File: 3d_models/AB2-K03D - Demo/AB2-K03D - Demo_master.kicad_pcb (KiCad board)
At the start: 2 copper layers, 223 parts

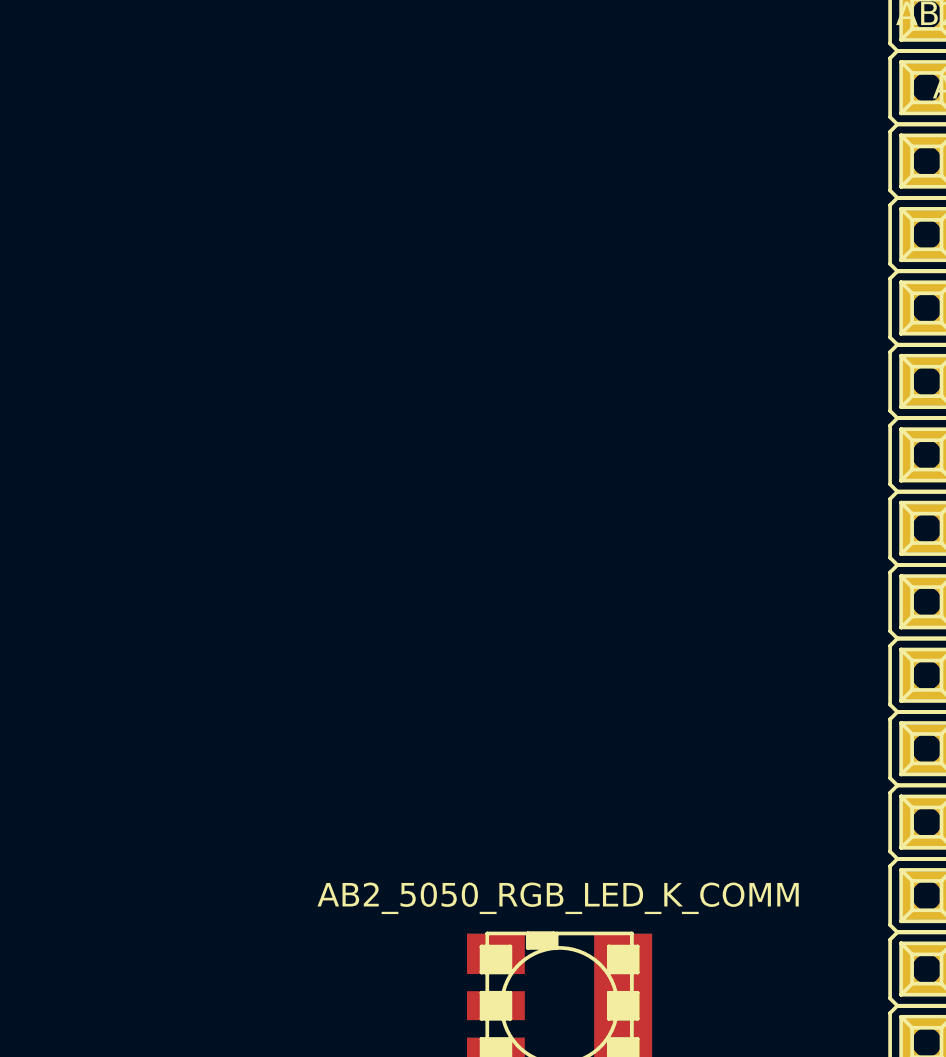
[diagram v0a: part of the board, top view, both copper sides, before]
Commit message: AB2-K03D: add 90' 4mm banana jacks blk/red to master
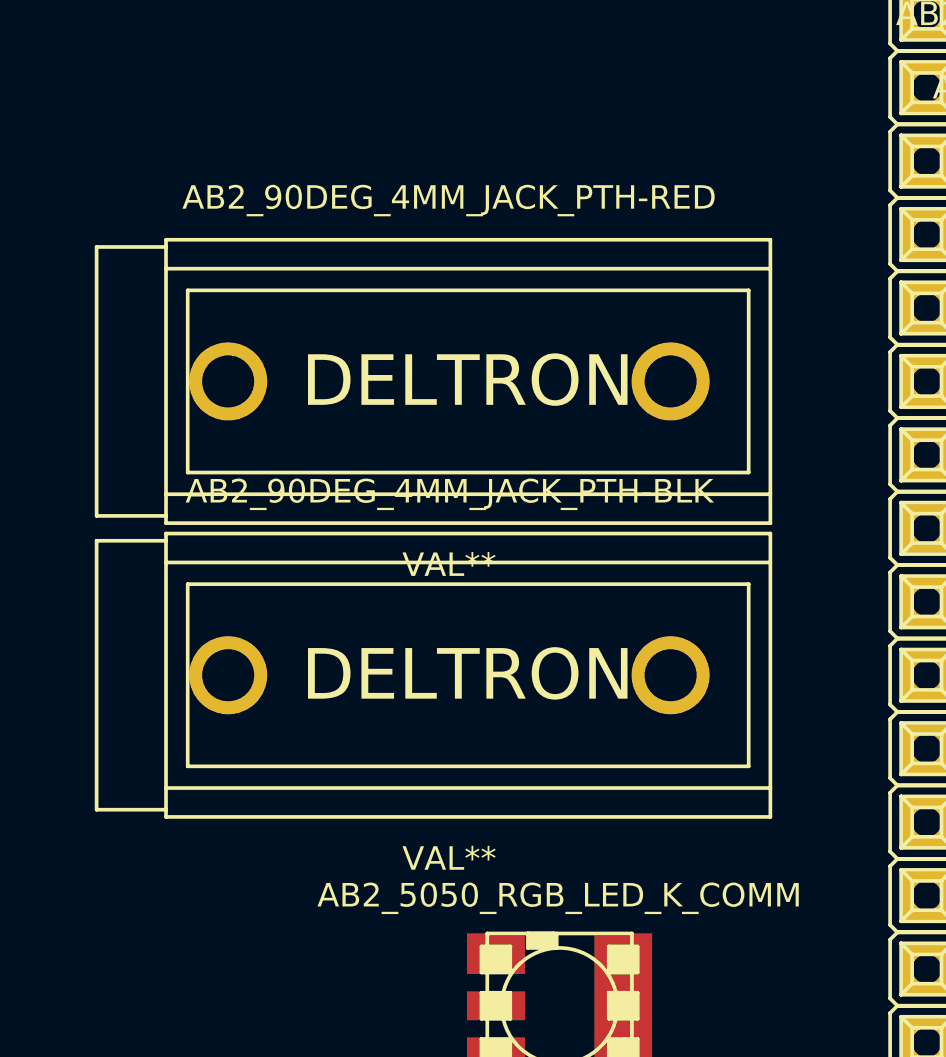
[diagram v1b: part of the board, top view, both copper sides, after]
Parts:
- added AB2_90DEG_4MM_JACK_PTH-BLK: VAL**, AB2_90DEG_4MM_JACK_PTH-BLK, F.Cu at (21.6, 156.2)
- added AB2_90DEG_4MM_JACK_PTH-RED: VAL**, AB2_90DEG_4MM_JACK_PTH-RED, F.Cu at (21.6, 146.1)
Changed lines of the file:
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@@
     (tracks 0)
     (zones 0)
-    (modules 223)
+    (modules 225)
     (nets 1)
   )
@@
     )
   )
+  (module AB2_90DEG_4MM_JACK_PTH-BLK (layer F.Cu)
+    (at 21.59 156.21)
+    (fp_text reference AB2_90DEG_4MM_JACK_PTH-BLK (at 0 -6.35) (layer F.SilkS)
+      (effects (font (size 0.8128 0.8128) (thickness 0.0762)))
+    )
+    (fp_text value VAL** (at 0 6.35) (layer F.SilkS)
+      (effects (font (size 0.8128 0.8128) (thickness 0.0762)))
+    )
+    (fp_line (start -9.05 -3.15) (end 10.35 -3.15) (layer F.SilkS) (width 0.127))
+    (fp_line (start 10.35 -3.15) (end 10.35 3.15) (layer F.SilkS) (width 0.127))
+    (fp_line (start 10.35 3.15) (end -9.05 3.15) (layer F.SilkS) (width 0.127))
+    (fp_line (start -9.05 3.15) (end -9.05 -3.15) (layer F.SilkS) (width 0.127))
+    (fp_line (start -9.8 3.9) (end 11.1 3.9) (layer F.SilkS) (width 0.127))
+    (fp_line (start -9.8 -3.9) (end 11.1 -3.9) (layer F.SilkS) (width 0.127))
+    (fp_text user DELTRON (at 0.635 0) (layer F.SilkS)
+      (effects (font (size 1.75 1.75) (thickness 0.2)))
+    )
+    (fp_line (start -9.8 -4.65) (end -12.2 -4.65) (layer F.SilkS) (width 0.127))
+    (fp_line (start -12.2 -4.65) (end -12.2 4.65) (layer F.SilkS) (width 0.127))
+    (fp_line (start -12.2 4.65) (end -9.8 4.65) (layer F.SilkS) (width 0.127))
+    (fp_line (start -9.8 -4.9) (end -9.8 4.9) (layer F.SilkS) (width 0.127))
+    (fp_line (start -9.8 4.9) (end 11.1 4.9) (layer F.SilkS) (width 0.127))
+    (fp_line (start 11.1 4.9) (end 11.1 -4.9) (layer F.SilkS) (width 0.127))
+    (fp_line (start 11.1 -4.9) (end -9.8 -4.9) (layer F.SilkS) (width 0.127))
+    (pad 1 thru_hole circle (at -7.65 0) (size 2.7 2.7) (drill 1.8)
+      (layers *.Cu *.Mask F.SilkS)
+    )
+    (pad 1 thru_hole circle (at 7.65 0) (size 2.7 2.7) (drill 1.8)
+      (layers *.Cu *.Mask F.SilkS)
+    )
+    (model ../3d_models/ab2_power/AB2_90DEG_4MM_JACK_PTH-BLK.wrl
+      (at (xyz 0 0 0))
+      (scale (xyz 0.3937 0.3937 0.3937))
+      (rotate (xyz 0 0 180))
+    )
+  )
+  (module AB2_90DEG_4MM_JACK_PTH-RED (layer F.Cu)
+    (at 21.59 146.05)
+    (fp_text reference AB2_90DEG_4MM_JACK_PTH-RED (at 0 -6.35) (layer F.SilkS)
+      (effects (font (size 0.8128 0.8128) (thickness 0.0762)))
+    )
+    (fp_text value VAL** (at 0 6.35) (layer F.SilkS)
+      (effects (font (size 0.8128 0.8128) (thickness 0.0762)))
+    )
+    (fp_line (start -9.05 -3.15) (end 10.35 -3.15) (layer F.SilkS) (width 0.127))
+    (fp_line (start 10.35 -3.15) (end 10.35 3.15) (layer F.SilkS) (width 0.127))
+    (fp_line (start 10.35 3.15) (end -9.05 3.15) (layer F.SilkS) (width 0.127))
+    (fp_line (start -9.05 3.15) (end -9.05 -3.15) (layer F.SilkS) (width 0.127))
+    (fp_line (start -9.8 3.9) (end 11.1 3.9) (layer F.SilkS) (width 0.127))
+    (fp_line (start -9.8 -3.9) (end 11.1 -3.9) (layer F.SilkS) (width 0.127))
+    (fp_text user DELTRON (at 0.635 0) (layer F.SilkS)
+      (effects (font (size 1.75 1.75) (thickness 0.2)))
+    )
+    (fp_line (start -9.8 -4.65) (end -12.2 -4.65) (layer F.SilkS) (width 0.127))
+    (fp_line (start -12.2 -4.65) (end -12.2 4.65) (layer F.SilkS) (width 0.127))
+    (fp_line (start -12.2 4.65) (end -9.8 4.65) (layer F.SilkS) (width 0.127))
+    (fp_line (start -9.8 -4.9) (end -9.8 4.9) (layer F.SilkS) (width 0.127))
+    (fp_line (start -9.8 4.9) (end 11.1 4.9) (layer F.SilkS) (width 0.127))
+    (fp_line (start 11.1 4.9) (end 11.1 -4.9) (layer F.SilkS) (width 0.127))
+    (fp_line (start 11.1 -4.9) (end -9.8 -4.9) (layer F.SilkS) (width 0.127))
+    (pad 1 thru_hole circle (at -7.65 0) (size 2.7 2.7) (drill 1.8)
+      (layers *.Cu *.Mask F.SilkS)
+    )
+    (pad 1 thru_hole circle (at 7.65 0) (size 2.7 2.7) (drill 1.8)
+      (layers *.Cu *.Mask F.SilkS)
+    )
+    (model ../3d_models/ab2_power/AB2_90DEG_4MM_JACK_PTH-RED.wrl
+      (at (xyz 0 0 0))
+      (scale (xyz 0.3937 0.3937 0.3937))
+      (rotate (xyz 0 0 180))
+    )
+  )

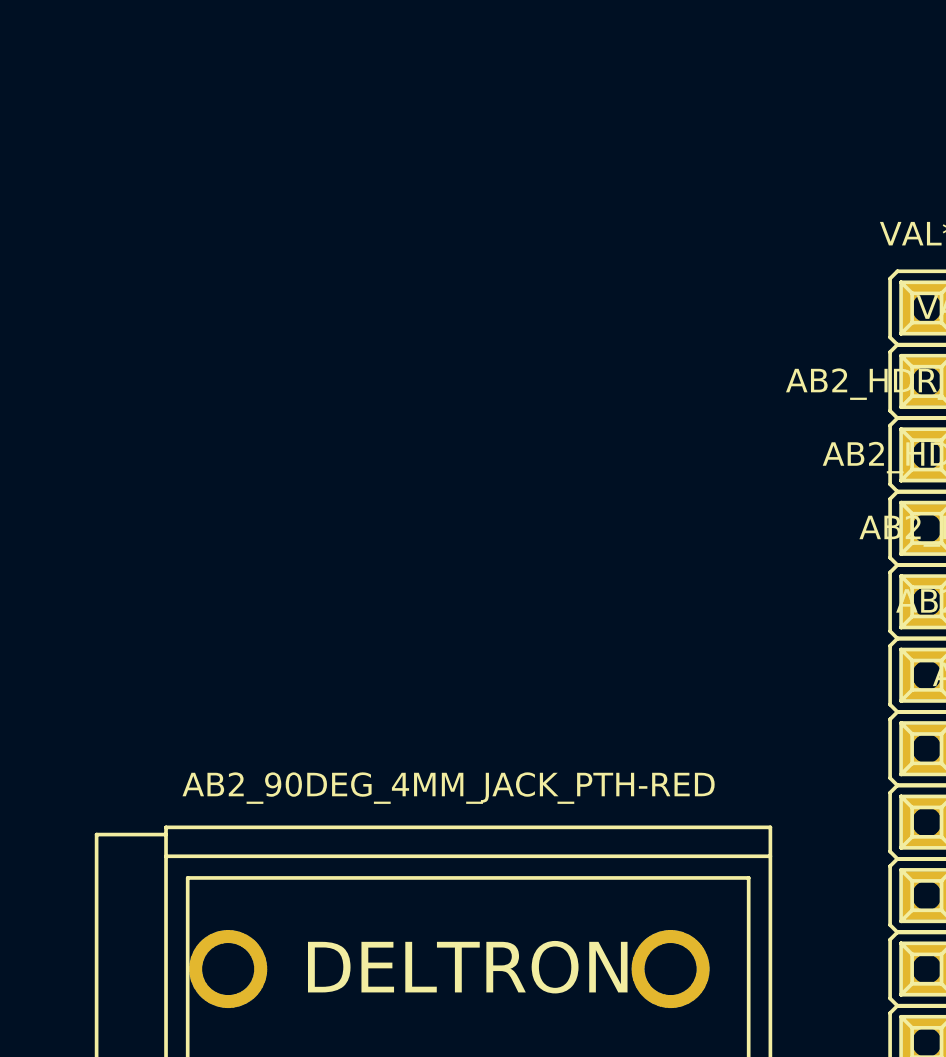
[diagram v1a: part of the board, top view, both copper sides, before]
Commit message: 3d_models: AB2-K03D: add 90' 4mm banana jacks
colors: blk/blu/red/yel
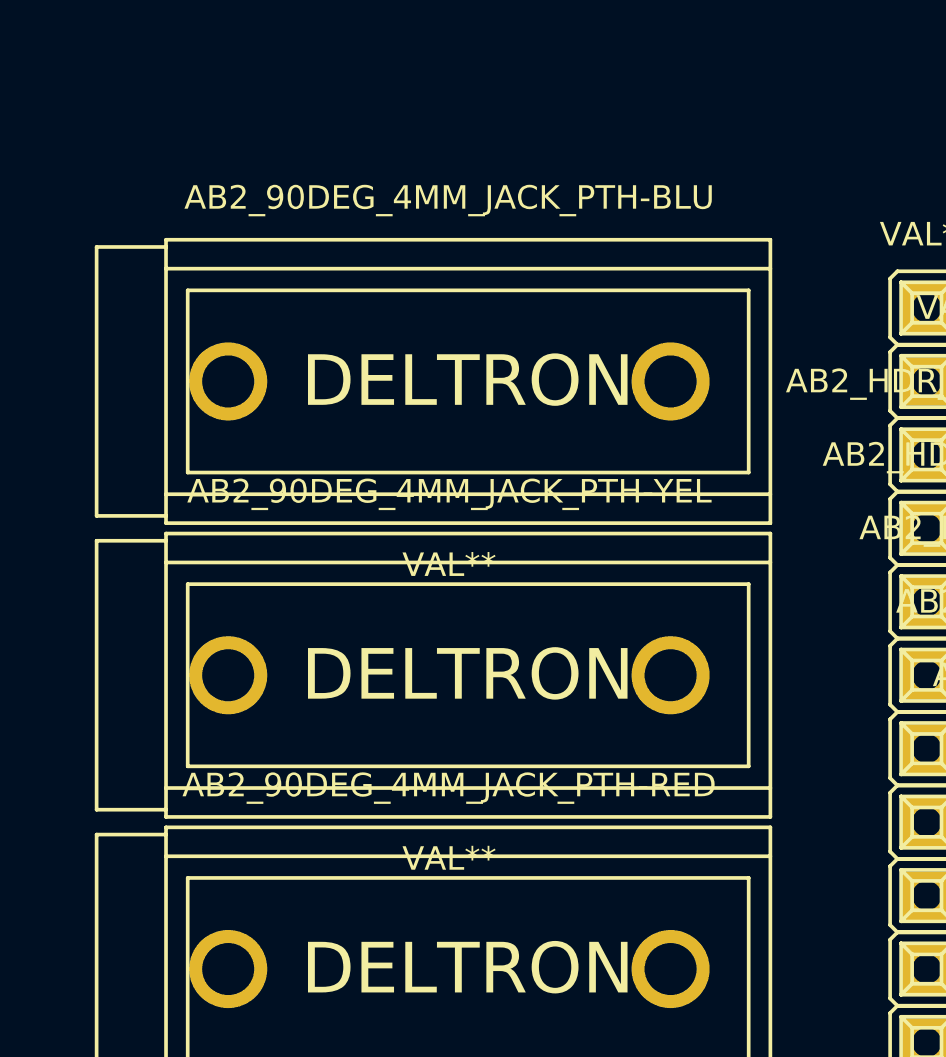
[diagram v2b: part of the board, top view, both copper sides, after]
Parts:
- added AB2_90DEG_4MM_JACK_PTH-BLU: VAL**, AB2_90DEG_4MM_JACK_PTH-BLU, F.Cu at (21.6, 125.7)
- added AB2_90DEG_4MM_JACK_PTH-YEL: VAL**, AB2_90DEG_4MM_JACK_PTH-YEL, F.Cu at (21.6, 135.9)
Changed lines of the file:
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@@
     (tracks 0)
     (zones 0)
-    (modules 225)
+    (modules 227)
     (nets 1)
   )
@@
       (at (xyz 0 0 0))
       (scale (xyz 0.3937 0.3937 0.3937))
+      (rotate (xyz 0 0 180))
+    )
+  )
+  (module AB2_90DEG_4MM_JACK_PTH-YEL (layer F.Cu)
+    (at 21.59 135.89)
+    (fp_text reference AB2_90DEG_4MM_JACK_PTH-YEL (at 0 -6.35) (layer F.SilkS)
+      (effects (font (size 0.8128 0.8128) (thickness 0.0762)))
+    )
+    (fp_text value VAL** (at 0 6.35) (layer F.SilkS)
+      (effects (font (size 0.8128 0.8128) (thickness 0.0762)))
+    )
+    (fp_line (start -9.05 -3.15) (end 10.35 -3.15) (layer F.SilkS) (width 0.127))
+    (fp_line (start 10.35 -3.15) (end 10.35 3.15) (layer F.SilkS) (width 0.127))
+    (fp_line (start 10.35 3.15) (end -9.05 3.15) (layer F.SilkS) (width 0.127))
+    (fp_line (start -9.05 3.15) (end -9.05 -3.15) (layer F.SilkS) (width 0.127))
+    (fp_line (start -9.8 3.9) (end 11.1 3.9) (layer F.SilkS) (width 0.127))
+    (fp_line (start -9.8 -3.9) (end 11.1 -3.9) (layer F.SilkS) (width 0.127))
+    (fp_text user DELTRON (at 0.635 0) (layer F.SilkS)
+      (effects (font (size 1.75 1.75) (thickness 0.2)))
+    )
+    (fp_line (start -9.8 -4.65) (end -12.2 -4.65) (layer F.SilkS) (width 0.127))
+    (fp_line (start -12.2 -4.65) (end -12.2 4.65) (layer F.SilkS) (width 0.127))
+    (fp_line (start -12.2 4.65) (end -9.8 4.65) (layer F.SilkS) (width 0.127))
+    (fp_line (start -9.8 -4.9) (end -9.8 4.9) (layer F.SilkS) (width 0.127))
+    (fp_line (start -9.8 4.9) (end 11.1 4.9) (layer F.SilkS) (width 0.127))
+    (fp_line (start 11.1 4.9) (end 11.1 -4.9) (layer F.SilkS) (width 0.127))
+    (fp_line (start 11.1 -4.9) (end -9.8 -4.9) (layer F.SilkS) (width 0.127))
+    (pad 1 thru_hole circle (at -7.65 0) (size 2.7 2.7) (drill 1.8)
+      (layers *.Cu *.Mask F.SilkS)
+    )
+    (pad 1 thru_hole circle (at 7.65 0) (size 2.7 2.7) (drill 1.8)
+      (layers *.Cu *.Mask F.SilkS)
+    )
+    (model ../3d_models/ab2_power/AB2_90DEG_4MM_JACK_PTH-YEL.wrl
+      (at (xyz 0 0 0))
+      (scale (xyz 0.3937 0.3937 0.3937))
+      (rotate (xyz 0 0 180))
+    )
+  )
+  (module AB2_90DEG_4MM_JACK_PTH-BLU (layer F.Cu)
+    (at 21.59 125.73)
+    (fp_text reference AB2_90DEG_4MM_JACK_PTH-BLU (at 0 -6.35) (layer F.SilkS)
+      (effects (font (size 0.8128 0.8128) (thickness 0.0762)))
+    )
+    (fp_text value VAL** (at 0 6.35) (layer F.SilkS)
+      (effects (font (size 0.8128 0.8128) (thickness 0.0762)))
+    )
+    (fp_line (start -9.05 -3.15) (end 10.35 -3.15) (layer F.SilkS) (width 0.127))
+    (fp_line (start 10.35 -3.15) (end 10.35 3.15) (layer F.SilkS) (width 0.127))
+    (fp_line (start 10.35 3.15) (end -9.05 3.15) (layer F.SilkS) (width 0.127))
+    (fp_line (start -9.05 3.15) (end -9.05 -3.15) (layer F.SilkS) (width 0.127))
+    (fp_line (start -9.8 3.9) (end 11.1 3.9) (layer F.SilkS) (width 0.127))
+    (fp_line (start -9.8 -3.9) (end 11.1 -3.9) (layer F.SilkS) (width 0.127))
+    (fp_text user DELTRON (at 0.635 0) (layer F.SilkS)
+      (effects (font (size 1.75 1.75) (thickness 0.2)))
+    )
+    (fp_line (start -9.8 -4.65) (end -12.2 -4.65) (layer F.SilkS) (width 0.127))
+    (fp_line (start -12.2 -4.65) (end -12.2 4.65) (layer F.SilkS) (width 0.127))
+    (fp_line (start -12.2 4.65) (end -9.8 4.65) (layer F.SilkS) (width 0.127))
+    (fp_line (start -9.8 -4.9) (end -9.8 4.9) (layer F.SilkS) (width 0.127))
+    (fp_line (start -9.8 4.9) (end 11.1 4.9) (layer F.SilkS) (width 0.127))
+    (fp_line (start 11.1 4.9) (end 11.1 -4.9) (layer F.SilkS) (width 0.127))
+    (fp_line (start 11.1 -4.9) (end -9.8 -4.9) (layer F.SilkS) (width 0.127))
+    (pad 1 thru_hole circle (at -7.65 0) (size 2.7 2.7) (drill 1.8)
+      (layers *.Cu *.Mask F.SilkS)
+    )
+    (pad 1 thru_hole circle (at 7.65 0) (size 2.7 2.7) (drill 1.8)
+      (layers *.Cu *.Mask F.SilkS)
+    )
+    (model ../3d_models/ab2_power/AB2_90DEG_4MM_JACK_PTH-BLU.wrl
+      (at (xyz 0 0 0))
+      (scale (xyz 0.3937 0.3937 0.3937))

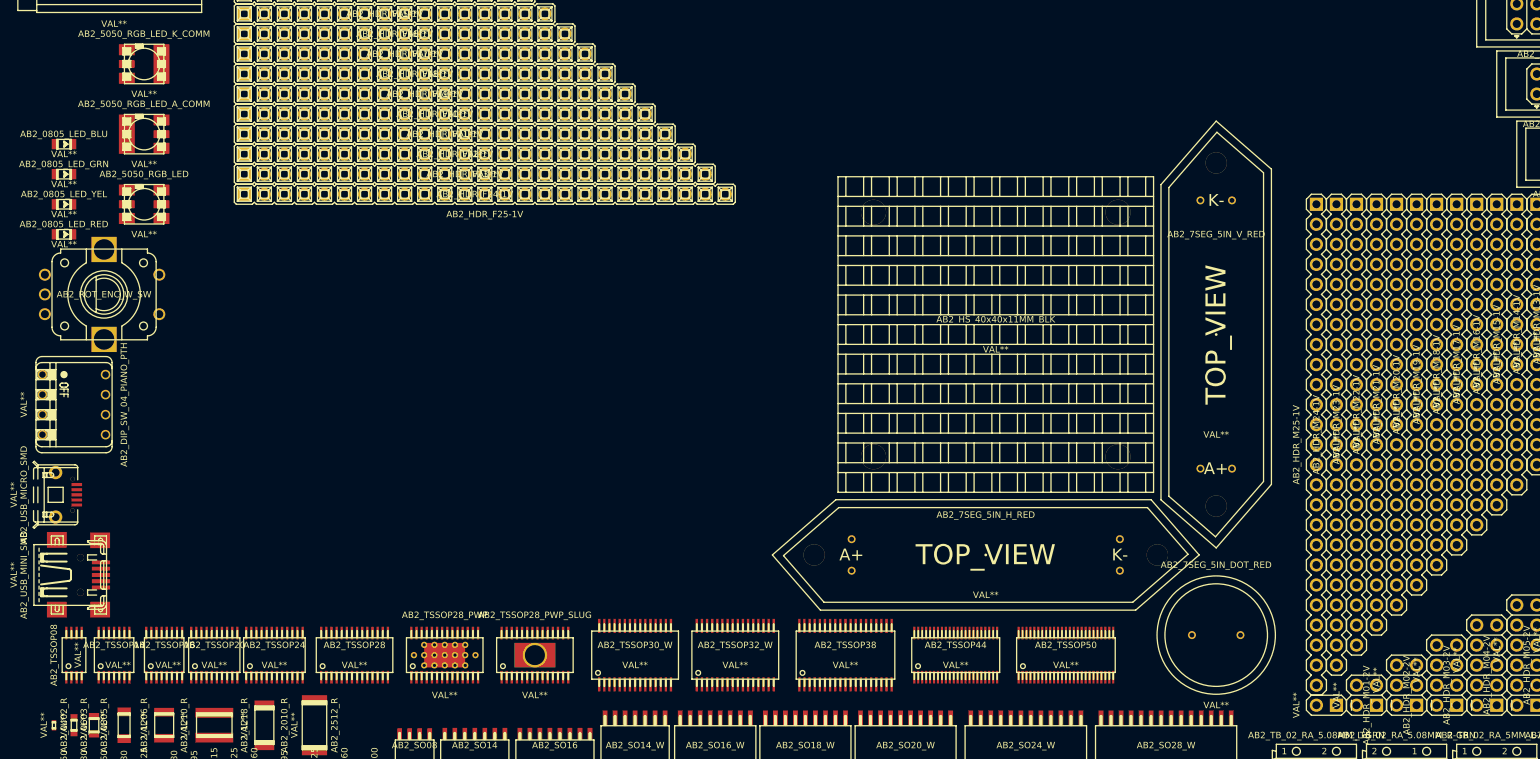
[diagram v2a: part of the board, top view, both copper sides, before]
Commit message: 3d: AB2-K03D: master: update all tssop pckgs
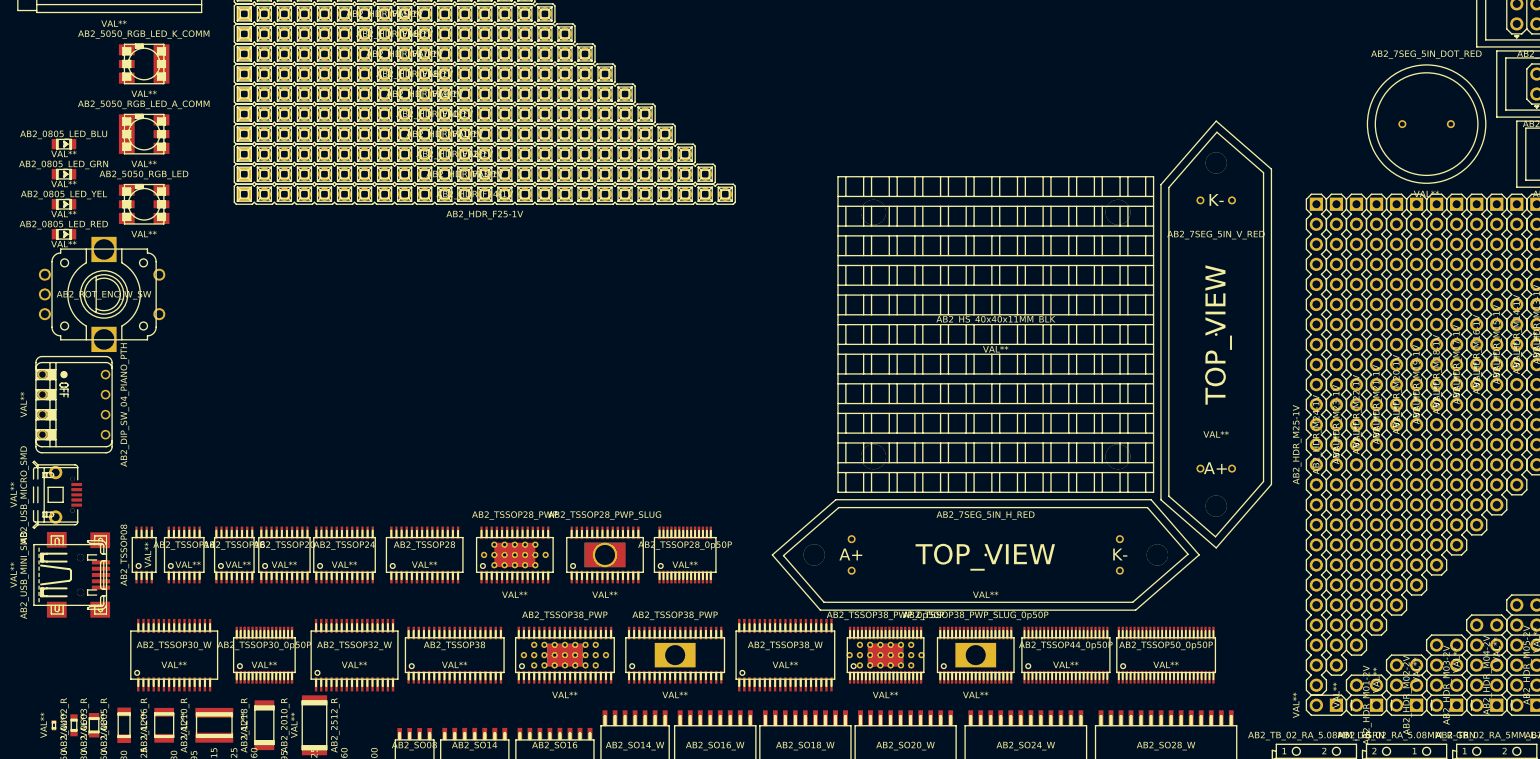
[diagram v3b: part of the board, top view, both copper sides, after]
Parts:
- removed AB2_TSSOP44: VAL**, AB2_TSSOP44
- removed AB2_TSSOP50: VAL**, AB2_TSSOP50
- added AB2_TSSOP28_0p50P: VAL**, AB2_TSSOP28_0p50P, F.Cu at (94.0, 229.9)
- added AB2_TSSOP30_0p50P: VAL**, AB2_TSSOP30_0p50P, F.Cu at (40.6, 242.6)
- added AB2_TSSOP38_PWP: VAL**, AB2_TSSOP38_PWP, F.Cu at (78.7, 242.6)
- added AB2_TSSOP38_PWP: VAL**, AB2_TSSOP38_PWP_SLUG, F.Cu at (92.7, 242.6)
- added AB2_TSSOP38_PWP_0p50P: VAL**, AB2_TSSOP38_PWP_0p50P, F.Cu at (119.4, 242.6)
- added AB2_TSSOP38_PWP_SLUG_0p50P: VAL**, AB2_TSSOP38_PWP_SLUG_0p50P, F.Cu at (130.8, 242.6)
- added AB2_TSSOP38_W: VAL**, AB2_TSSOP38_W, F.Cu at (106.7, 242.6)
- added AB2_TSSOP44_0p50P: VAL**, AB2_TSSOP44_0p50P, F.Cu at (142.2, 242.6)
- added AB2_TSSOP50_0p50P: VAL**, AB2_TSSOP50_0p50P, F.Cu at (154.9, 242.6)
- AB2_TSSOP38: footprint AB2_TSSOP38_W -> AB2_TSSOP38
- moved AB2_7SEG_5IN_DOT_RED 70.0 mm to (188.0, 175.3)
- moved AB2_TSSOP30_W 58.4 mm to (29.2, 242.6)
- moved AB2_TSSOP38 49.5 mm to (64.8, 242.6)
- moved AB2_TSSOP32_W 48.3 mm to (52.1, 242.6)
- moved AB2_TSSOP14 15.5 mm to (30.5, 229.9)
- moved AB2_TSSOP20 15.5 mm to (43.2, 229.9)
- moved AB2_TSSOP24 15.5 mm to (50.8, 229.9)
- moved AB2_TSSOP28 15.5 mm to (61.0, 229.9)
- moved AB2_TSSOP28_PWP 15.5 mm to (72.4, 229.9)
- moved AB2_TSSOP08 15.5 mm to (25.4, 229.9)
- moved AB2_TSSOP16 15.5 mm to (36.8, 229.9)
- moved AB2_TSSOP28_PWP_SLUG 15.5 mm to (83.8, 229.9)
